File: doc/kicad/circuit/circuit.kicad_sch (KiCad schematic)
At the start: 17 parts, among them J1 4X4 Button Matrix, J1.1 2X2 Button Matrix A, J1.1.1 Button 1, J1.1.2 Button 2, J1.1.3 Button 5, J1.1.4 Button 6, J1.2 2X2 Button Matrix B, J1.2.1 Button 3, J1.2.2 Button 4, J1.3 2X2 Button Matrix C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

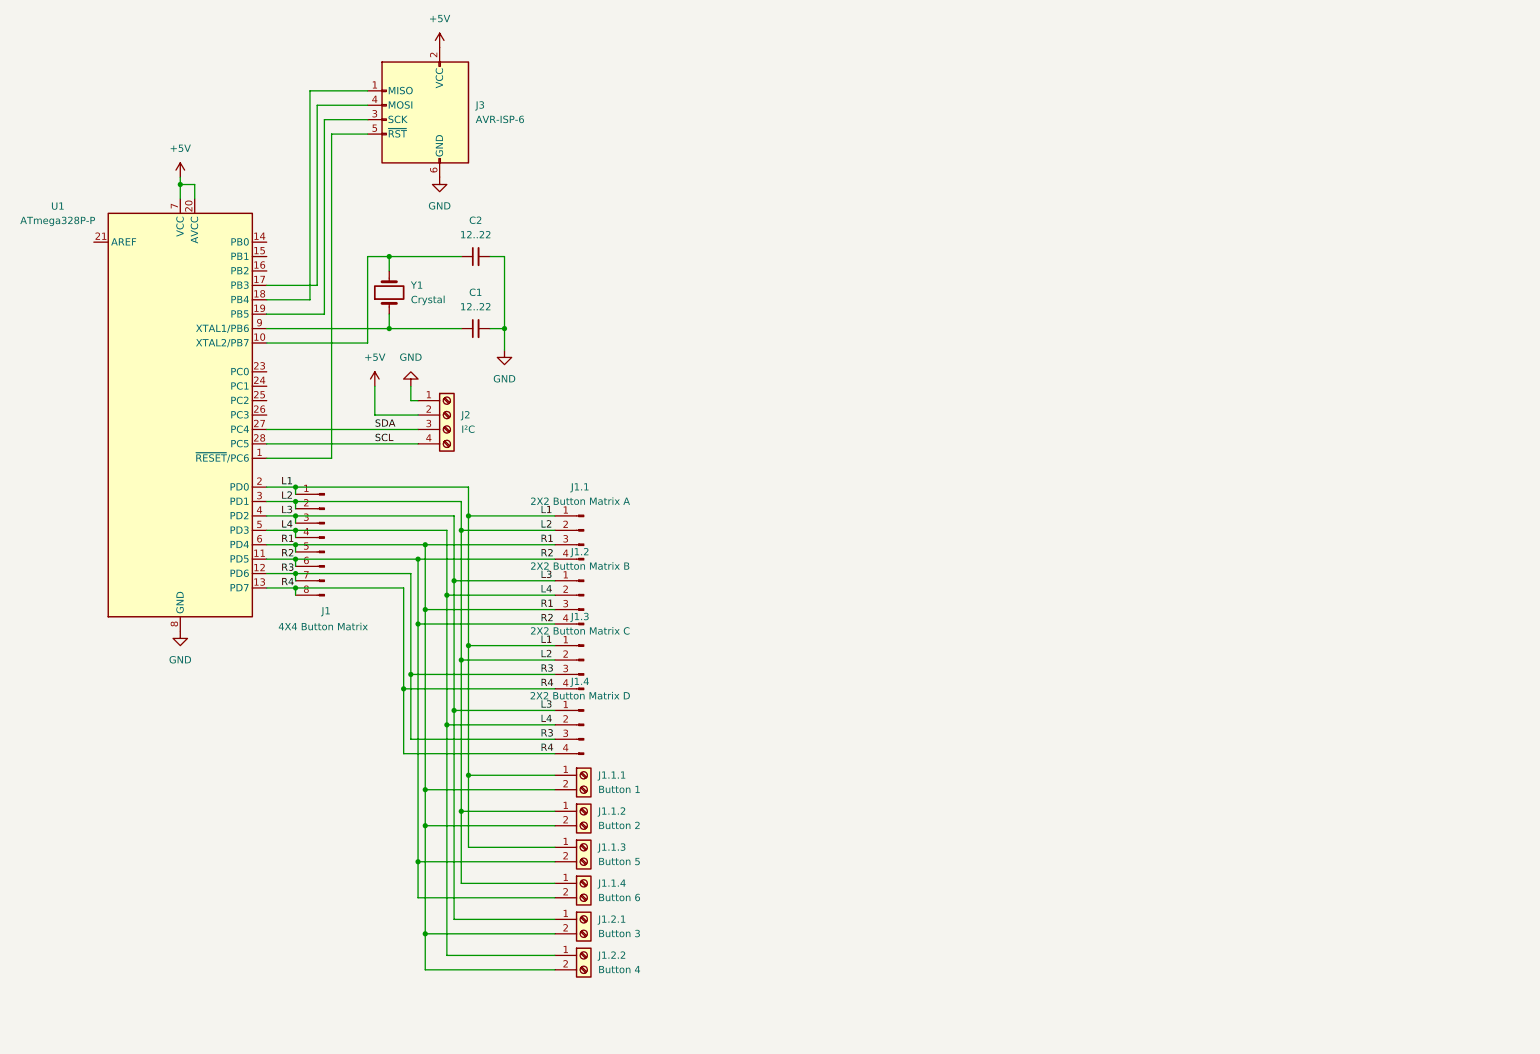
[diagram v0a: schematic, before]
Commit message: first test runs good in arduino uno envirement
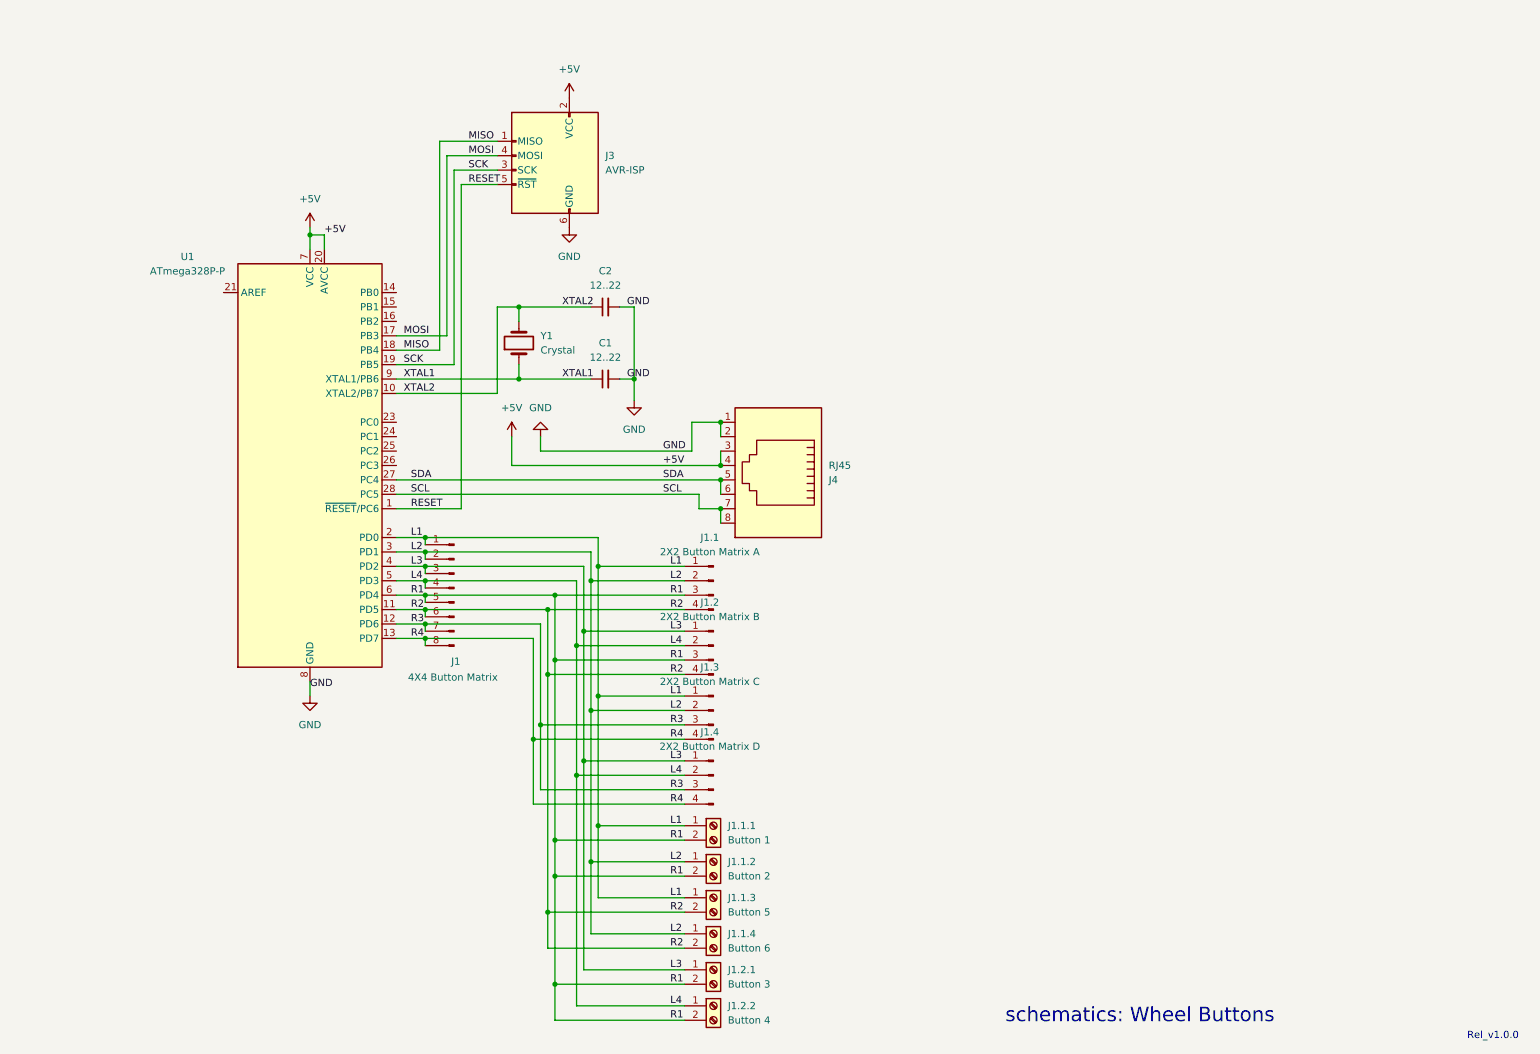
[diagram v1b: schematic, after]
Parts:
- removed J2: I²C, TerminalBlock:TerminalBlock_Xinya_XY308-2.54-4P_1x04_P2.54mm_Horizontal, symbol Connector:Screw_Terminal_01x04
- added J4: RJ45, Connector_RJ:RJ45_Molex_0855135013_Vertical, symbol Connector:RJ45
- J1: value 4X4 Button Matrix -> 4X4 Button Matrix
- J3: value AVR-ISP-6 -> AVR-ISP
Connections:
- net +5V: now also J4.3, J4.4
- net GND: now also J4.1, J4.2
- net SCL: now also J4.7, J4.8
- net SDA: now also J4.5, J4.6
- net XTAL1: now reaches C1.1, U1.9 (XTAL1/PB6), Y1.1
- net XTAL2: now reaches C2.1, U1.10 (XTAL2/PB7), Y1.2
- net MISO: now reaches J3.1 (MISO), U1.18 (PB4)
- net SCK: now reaches J3.3 (SCK), U1.19 (PB5)
- net MOSI: now reaches J3.4 (MOSI), U1.17 (PB3)
- net RESET: now reaches J3.5 (~{RST}), U1.1 (~{RESET}/PC6)
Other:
- note added: "Rel_v1.0.0"
- note added: "schematics: Wheel Buttons"
- moved on the sheet: C1, C2, J1, J1.1, J1.1.1, J1.1.2, J1.1.3, J1.1.4, J1.2, J1.2.1, J1.2.2, J1.3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

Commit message: add some comments and update pcb
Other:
- note removed: "Rel_v1.0.0"
- note removed: "schematics: Wheel Buttons"
- company: (none) -> https://github.com/lusmdl
- title: (none) -> wheele buttons
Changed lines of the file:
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@@
 	(generator_version "8.0")
 	(paper "A4")
+	(title_block
+		(title "wheele buttons")
+		(date "2024-07-18")
+		(rev "v1.0.0")
+		(company "https://github.com/lusmdl")
+	)
 	(junction
 		(at 86.36 115.57)
@@
 		)
 	)
-	(text "Rel_v1.0.0"
-		(exclude_from_sim no)
-		(at 274.574 193.294 0)
-		(effects
-			(font
-				(size 1.27 1.27)
-			)
-		)
-	)
-	(text "schematics: Wheel Buttons"
-		(exclude_from_sim no)
-		(at 212.344 189.738 0)
-		(effects
-			(font
-				(size 2.54 2.54)
-			)
-			(href "https://github.com/lusmdl/MySimRacingWheeleButtons")
-		)
-	)

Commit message: finish PCBA
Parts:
- added SW1: Reset, Button_Switch_SMD:SW_Push_1P1T_NO_6x6mm_H9.5mm, symbol Switch:SW_Push
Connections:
- net GND: now also SW1.2
- net RESET: now also SW1.1
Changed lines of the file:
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@@
+	)
+	(junction
+		(at 106.68 90.17)
+		(diameter 0)
+		(color 0 0 0 0)
 	)
 	(junction
@@
 	)
 	(junction
+		(at 92.71 100.33)
+		(diameter 0)
+		(color 0 0 0 0)
+	)
+	(junction
 		(at 86.36 105.41)
 		(diameter 0)
@@
 	(wire
 		(pts
+			(xy 106.68 100.33) (xy 106.68 90.17)
+		)
+		(stroke
+			(width 0)
+			(type default)
+		)
+	)
+	(wire
+		(pts
 			(xy 86.36 105.41) (xy 116.84 105.41)
 		)
@@
 	(wire
 		(pts
+			(xy 106.68 90.17) (xy 133.35 90.17)
+		)
+		(stroke
+			(width 0)
+			(type default)
+		)
+	)
+	(wire
+		(pts
 			(xy 132.08 140.97) (xy 105.41 140.97)
 		)
@@
 	(wire
 		(pts
-			(xy 106.68 90.17) (xy 133.35 90.17)
-		)
-		(stroke
-			(width 0)
-			(type default)
-		)
-	)
-	(wire
-		(pts
 			(xy 132.08 177.8) (xy 107.95 177.8)
 		)
@@
 		(pts
 			(xy 116.84 110.49) (xy 132.08 110.49)
+		)
+		(stroke
+			(width 0)
+			(type default)
+		)
+	)
+	(wire
+		(pts
+			(xy 96.52 100.33) (xy 92.71 100.33)
 		)
 		(stroke
@@
 					(unit 1)
 				)
+			)
+		)
+	)
+	(symbol
+		(lib_id "Switch:SW_Push")
+		(at 101.6 100.33 0)
+		(unit 1)
+		(exclude_from_sim no)
+		(in_bom yes)
+		(on_board yes)
+		(dnp no)
+		(property "Reference" "SW1"
+			(at 101.6 102.108 0)
+			(effects
+				(font
+					(size 1.27 1.27)
+				)
+			)
+		)
+		(property "Value" "Reset"
+			(at 108.204 102.108 0)
+			(effects
+				(font
+					(size 1.27 1.27)
+				)
+			)
+		)
+		(property "Footprint" "Button_Switch_SMD:SW_Push_1P1T_NO_6x6mm_H9.5mm"
+			(at 101.6 95.25 0)
+			(effects
+				(font
+					(size 1.27 1.27)
+				)
+				(hide yes)
+			)
+		)
+		(property "Datasheet" "~"
+			(at 101.6 95.25 0)
+			(effects
+				(font
+					(size 1.27 1.27)
+				)
+				(hide yes)
+			)
+		)
+		(property "Description" "Push button switch, generic, two pins"
+			(at 101.6 100.33 0)
+			(effects
+				(font
+					(size 1.27 1.27)
+				)
+				(hide yes)
+			)
+		)
+		(pin "1"
+		)
+		(pin "2"
+		)
+		(instances
+			(project ""
+				(path "/edf5049a-0fa6-4e51-97b2-c2c53b61158b"
+					(reference "SW1")
+					(unit 1)
+				)

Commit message: refactor pcb
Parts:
- C1, C2: footprint Capacitor_SMD:C_0603_1608Metric_Pad1.08x0.95mm_HandSolder -> Capacitor_SMD:C_0402_1005Metric
- J1: footprint Connector_PinHeader_2.54mm:PinHeader_1x08_P2.54mm_Vertical_SMD_Pin1Left -> Connector_PinHeader_2.54mm:PinHeader_2x04_P2.54mm_Vertical_SMD
- J1.1, J1.2, J1.3, J1.4: footprint Connector_PinHeader_2.54mm:PinHeader_1x04_P2.54mm_Vertical_SMD_Pin1Left -> Connector_PinHeader_2.54mm:PinHeader_2x02_P2.54mm_Vertical_SMD
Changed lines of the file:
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@@
 			)
 		)
-		(property "Footprint" "Capacitor_SMD:C_0603_1608Metric_Pad1.08x0.95mm_HandSolder"
+		(property "Footprint" "Capacitor_SMD:C_0402_1005Metric"
 			(at 118.11 64.77 0)
 			(effects
@@
 			)
 		)
-		(property "Footprint" "Connector_PinHeader_2.54mm:PinHeader_1x04_P2.54mm_Vertical_SMD_Pin1Left"
+		(property "Footprint" "Connector_PinHeader_2.54mm:PinHeader_2x02_P2.54mm_Vertical_SMD"
 			(at 137.16 135.89 0)
 			(effects
@@
 			)
 		)
-		(property "Footprint" "Connector_PinHeader_2.54mm:PinHeader_1x04_P2.54mm_Vertical_SMD_Pin1Left"
+		(property "Footprint" "Connector_PinHeader_2.54mm:PinHeader_2x02_P2.54mm_Vertical_SMD"
 			(at 137.16 124.46 0)
 			(effects
@@
 			)
 		)
-		(property "Footprint" "Connector_PinHeader_2.54mm:PinHeader_1x08_P2.54mm_Vertical_SMD_Pin1Left"
+		(property "Footprint" "Connector_PinHeader_2.54mm:PinHeader_2x04_P2.54mm_Vertical_SMD"
 			(at 91.44 114.3 0)
 			(effects
@@
 			)
 		)
-		(property "Footprint" "Connector_PinHeader_2.54mm:PinHeader_1x04_P2.54mm_Vertical_SMD_Pin1Left"
+		(property "Footprint" "Connector_PinHeader_2.54mm:PinHeader_2x02_P2.54mm_Vertical_SMD"
 			(at 137.16 113.03 0)
 			(effects
@@
 			)
 		)
-		(property "Footprint" "Capacitor_SMD:C_0603_1608Metric_Pad1.08x0.95mm_HandSolder"
+		(property "Footprint" "Capacitor_SMD:C_0402_1005Metric"
 			(at 118.11 77.47 0)
 			(effects
@@
 			)
 		)
-		(property "Footprint" "Connector_PinHeader_2.54mm:PinHeader_1x04_P2.54mm_Vertical_SMD_Pin1Left"
+		(property "Footprint" "Connector_PinHeader_2.54mm:PinHeader_2x02_P2.54mm_Vertical_SMD"
 			(at 137.16 147.32 0)
 			(effects
